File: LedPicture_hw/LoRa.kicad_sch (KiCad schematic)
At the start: 33 parts

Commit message: + OS works + Antenna tuned
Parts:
- C43: value *** -> 2pF
- C44: value *** -> DoNotMount
- L7: value *** -> 6.8nH
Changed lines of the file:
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@@
     (in_bom yes) (on_board yes)
     (property "Reference" "L7" (id 0) (at 242.57 84.6836 90))
-    (property "Value" "***" (id 1) (at 242.57 86.995 90))
+    (property "Value" "6.8nH" (id 1) (at 242.57 86.995 90))
     (property "Footprint" "Inductors:IND_0402" (id 2) (at 242.316 88.646 90)
       (effects (font (size 1.016 1.016)) hide)
@@
       (effects (font (size 1.27 1.27)) (justify left))
     )
-    (property "Value" "***" (id 1) (at 232.41 93.98 0)
+    (property "Value" "2pF" (id 1) (at 232.41 93.98 0)
       (effects (font (size 1.27 1.27)) (justify left))
     )
@@
       (effects (font (size 1.27 1.27)) (justify left))
     )
-    (property "Value" "***" (id 1) (at 247.65 93.98 0)
-      (effects (font (size 1.27 1.27)) (justify left))
-    )
+    (property "Value" "DoNotMount" (id 1) (at 247.65 93.98 0)
+      (effects (font (size 1.27 1.27)) (justify left))
+    )

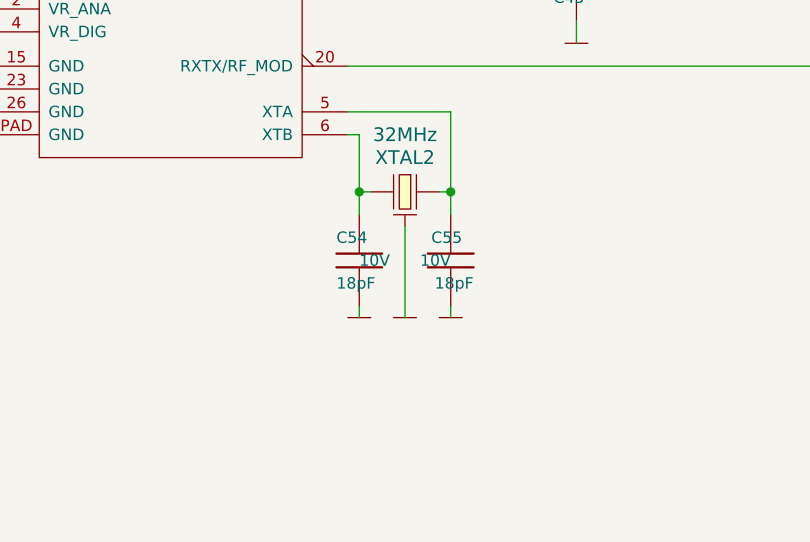
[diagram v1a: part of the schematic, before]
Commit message: First LORA Rx ok
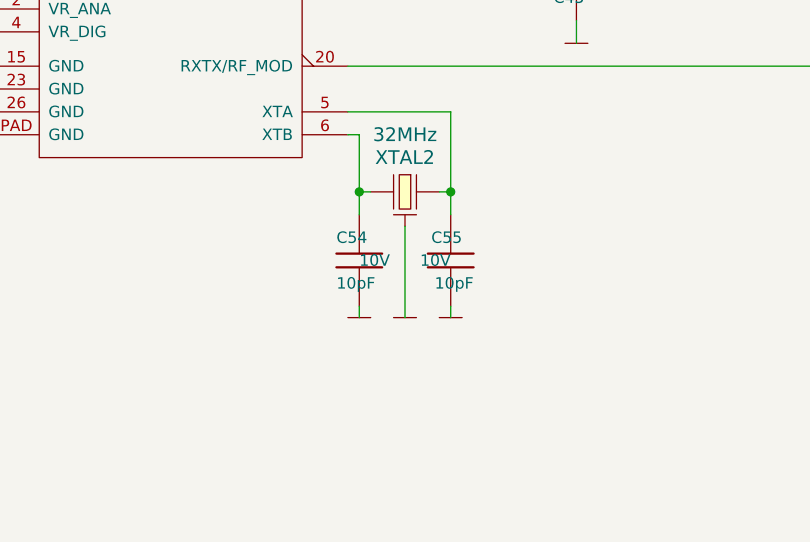
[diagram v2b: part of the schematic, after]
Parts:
- C54, C55: value 18pF -> 10pF
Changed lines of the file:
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@@
       (effects (font (size 1.27 1.27)) (justify left))
     )
-    (property "Value" "18pF" (id 1) (at 114.3 135.89 0)
+    (property "Value" "10pF" (id 1) (at 114.3 135.89 0)
       (effects (font (size 1.27 1.27)) (justify left))
     )
@@
       (effects (font (size 1.27 1.27)) (justify left))
     )
-    (property "Value" "18pF" (id 1) (at 129.54 135.89 0)
+    (property "Value" "10pF" (id 1) (at 129.54 135.89 0)
       (effects (font (size 1.27 1.27)) (justify left))
     )
